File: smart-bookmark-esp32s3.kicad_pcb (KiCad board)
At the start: 4 copper layers, 37 x 52 mm, 52 parts, among them J1 USB-C 16P, Q1 FS8205A, Q2 AO3401A, Q3 2N7002, SW1 TS-1088-AR02016, U1 ESP32-S3-MINI-1-N8, U2 USBLC6-2SC6, U3 MCP73832T-2ACI/OT, U4 DW01A, U5 RT9080-33GJ5, U6 W25Q128JVPIQ

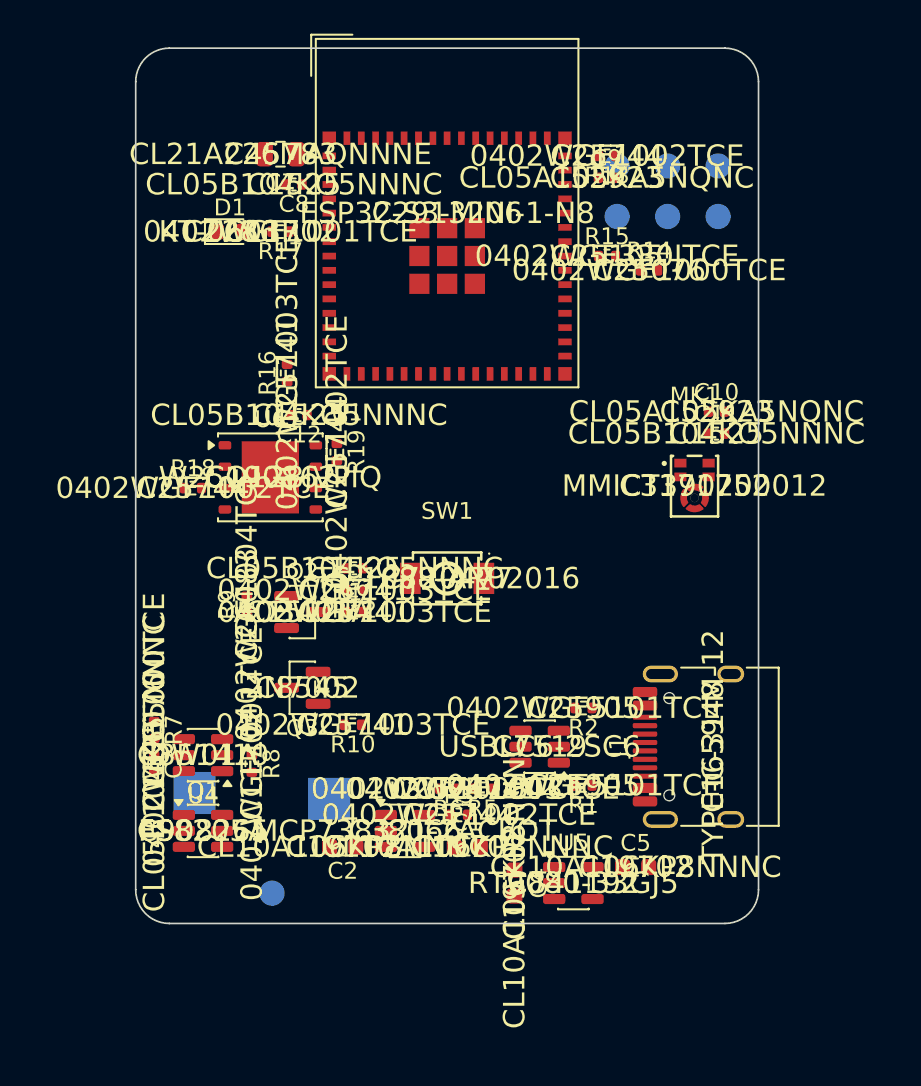
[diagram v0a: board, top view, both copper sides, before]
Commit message: Placement: add missing 3D models, clean up silkscreen
Module, USB-C and mic now have models; MPN/LCSC fields hidden; designators on silk only for ICs/connectors, passives on Fab; back-side pad labels. Module model offset and J1 label position still need a small nudge.

Co-Authored-By: Claude Opus 5.5 <noreply@anthropic.com>
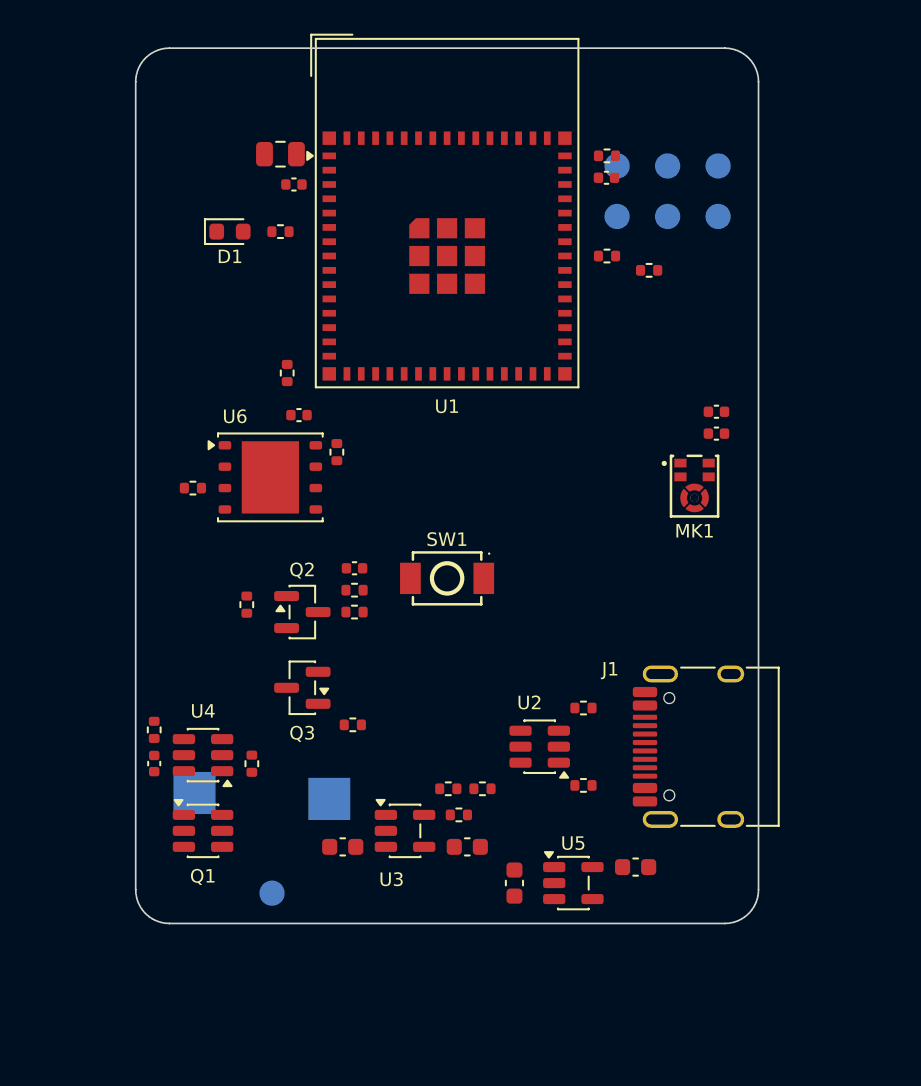
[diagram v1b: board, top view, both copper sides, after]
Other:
- board text added: "3V3"
- board text added: "BAT+"
- board text added: "BAT-"
- board text added: "BOOT"
- board text added: "CELL AREA - NO PADS"
- board text added: "EN"
- board text added: "GND"
- board text added: "RX"
- board text added: "SMART BOOKMARK REV A"
- board text added: "TX"
- board text added: "VBAT"

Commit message: Route the board, DRC clean, JLCPCB fab package
Hand-routed 4-layer board (GND and +3V3 inner planes). DRC 0 errors, 0 unconnected, 0 parity; two expected lib_footprint_mismatch warnings. Module moved 0.45 mm down (real part is longer than the footprint outline). Mic port hole made non-plated with a footprint-local clearance rule. Gerbers, BOM, CPL, STEP and PDFs in fab/.

Co-Authored-By: Claude Opus 5.5 <noreply@anthropic.com>
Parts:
- moved C8 0.45 mm to (109.4, 78.5)
- moved C9 0.45 mm to (128.0, 78.2)
- moved R14 0.45 mm to (130.5, 83.7)
- moved R15 0.45 mm to (128.0, 82.8)
- moved R16 0.45 mm to (109.0, 89.8)
- moved U1 0.45 mm to (118.5, 80.2)
- moved D1 0.45 mm to (105.6, 81.3)
- moved R13 0.45 mm to (128.0, 76.8)
- moved R17 0.45 mm to (108.6, 81.3)
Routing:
- net +BATT: track 0.00 -> 52.3 mm, vias 0 -> 3
- net GND: track 0.00 -> 42.1 mm, vias 0 -> 89
- net /USB_DN: track 0.00 -> 36.5 mm
- net /USB_DP: track 0.00 -> 31.9 mm
- net /BOOT: track 0.00 -> 31.0 mm, vias 0 -> 1
- net /VBUS_DET: track 0.00 -> 29.8 mm
- net VBUS: track 0.00 -> 28.3 mm, vias 0 -> 5
- net /CHG_STAT_N: track 0.00 -> 26.6 mm
- net /BAT_SENSE_EN: track 0.00 -> 25.4 mm
- net /BTN_N: track 0.00 -> 24.9 mm, vias 0 -> 2
- net /BAT_ADC: track 0.00 -> 23.4 mm, vias 0 -> 2
- net /audio/MIC_CLK_R: track 0.00 -> 22.1 mm
- net /MIC_DATA: track 0.00 -> 17.0 mm
- net /FLASH_MISO: track 0.00 -> 16.2 mm
- net +3V3: track 0.00 -> 16.1 mm, vias 0 -> 6
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- added copper zone on In2.Cu, net +3V3
- added copper zone on B.Cu, net GND
- added copper zone on F.Cu, net GND
- added copper zone on In1.Cu, net GND

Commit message: Populate U6 flash, add silkscreen section labels, design brief
U6 and its passives are now fitted (BOM 24 lines / 43 parts). Top silk names each section; cell outline on the back. docs/designBrief.html generated. ERC and DRC unchanged: 0 errors. Firmware does not use U6 yet.

Co-Authored-By: Claude Opus 5.5 <noreply@anthropic.com>
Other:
- board text added: "16MB FLASH"
- board text added: "3V3 REG"
- board text added: "ANTENNA"
- board text added: "BATT"
- board text added: "CELL 25 x 30"
- board text added: "CHARGER"
- board text added: "ESP32-S3 BLE"
- board text added: "KEEP CLEAR"
- board text added: "MIC"
- board text added: "PROTECT"
- board text added: "RECORD"
- board text added: "SENSE"
- board text added: "STATUS LED"
- board text added: "USB-C"
